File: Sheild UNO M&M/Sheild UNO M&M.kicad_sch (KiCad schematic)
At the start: 20 parts, among them J1 Power, J2 Analog, J3 Digital/PWM, J4 Digital/PWM, J5 Conn_01x02, J6 Conn_01x02, U1 HC05, U2 MCP41050, U4 LTC1050

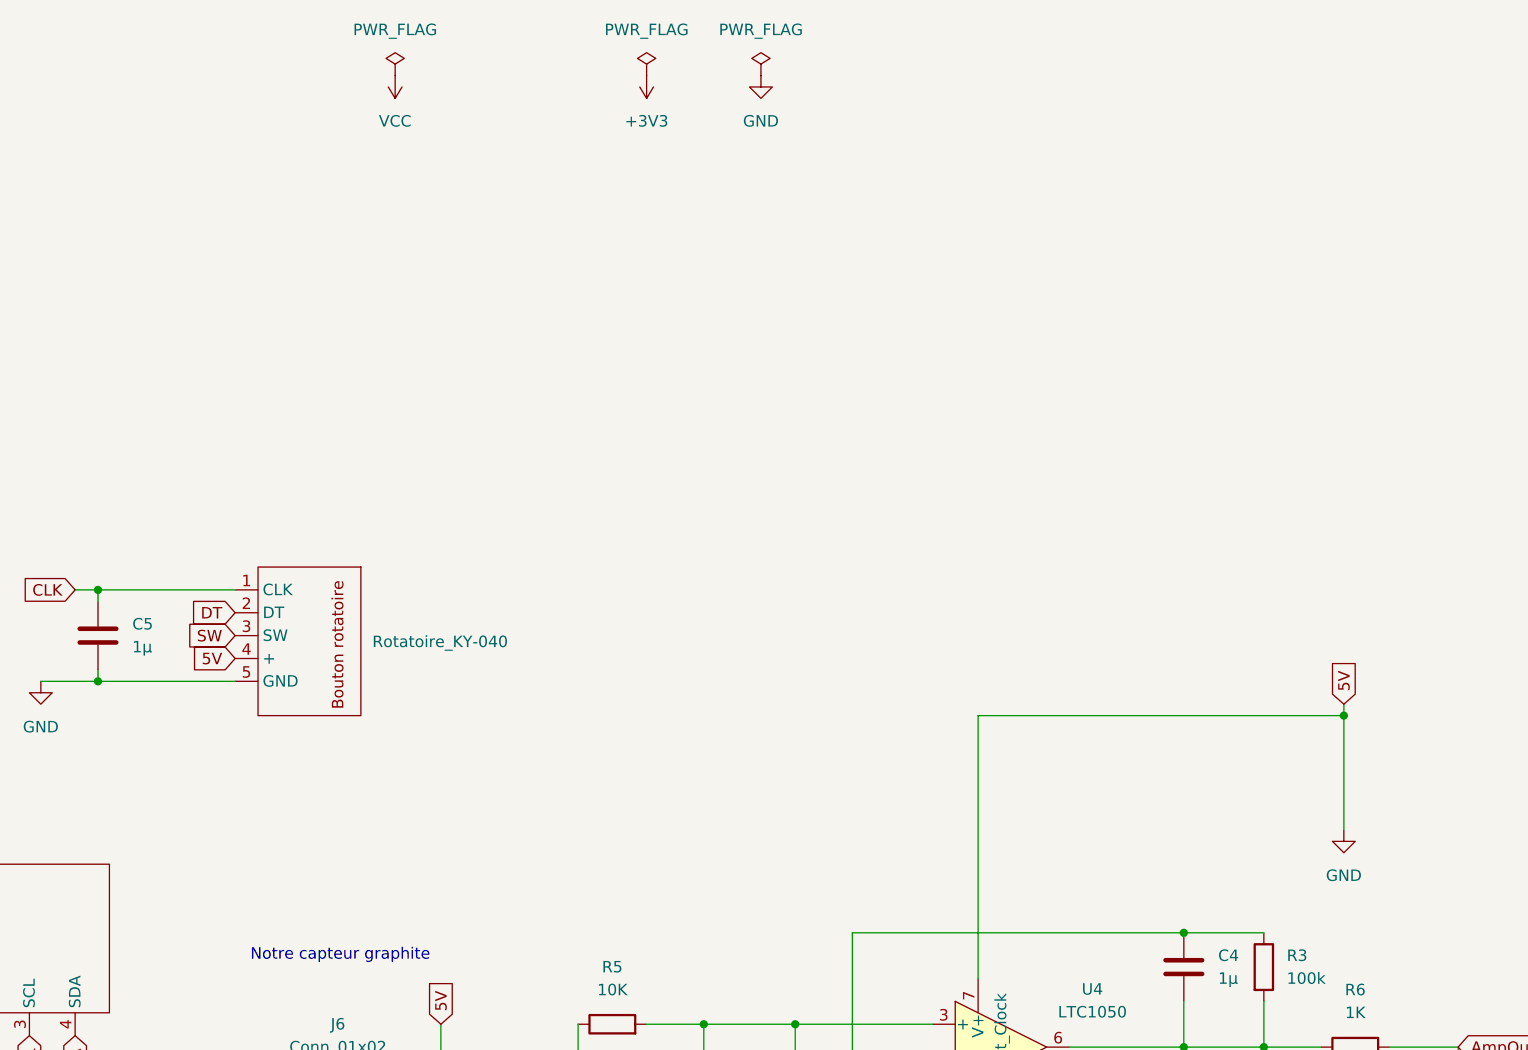
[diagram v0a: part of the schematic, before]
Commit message: Correction de l'erreur du GND connecté au 5V, continuer le routage
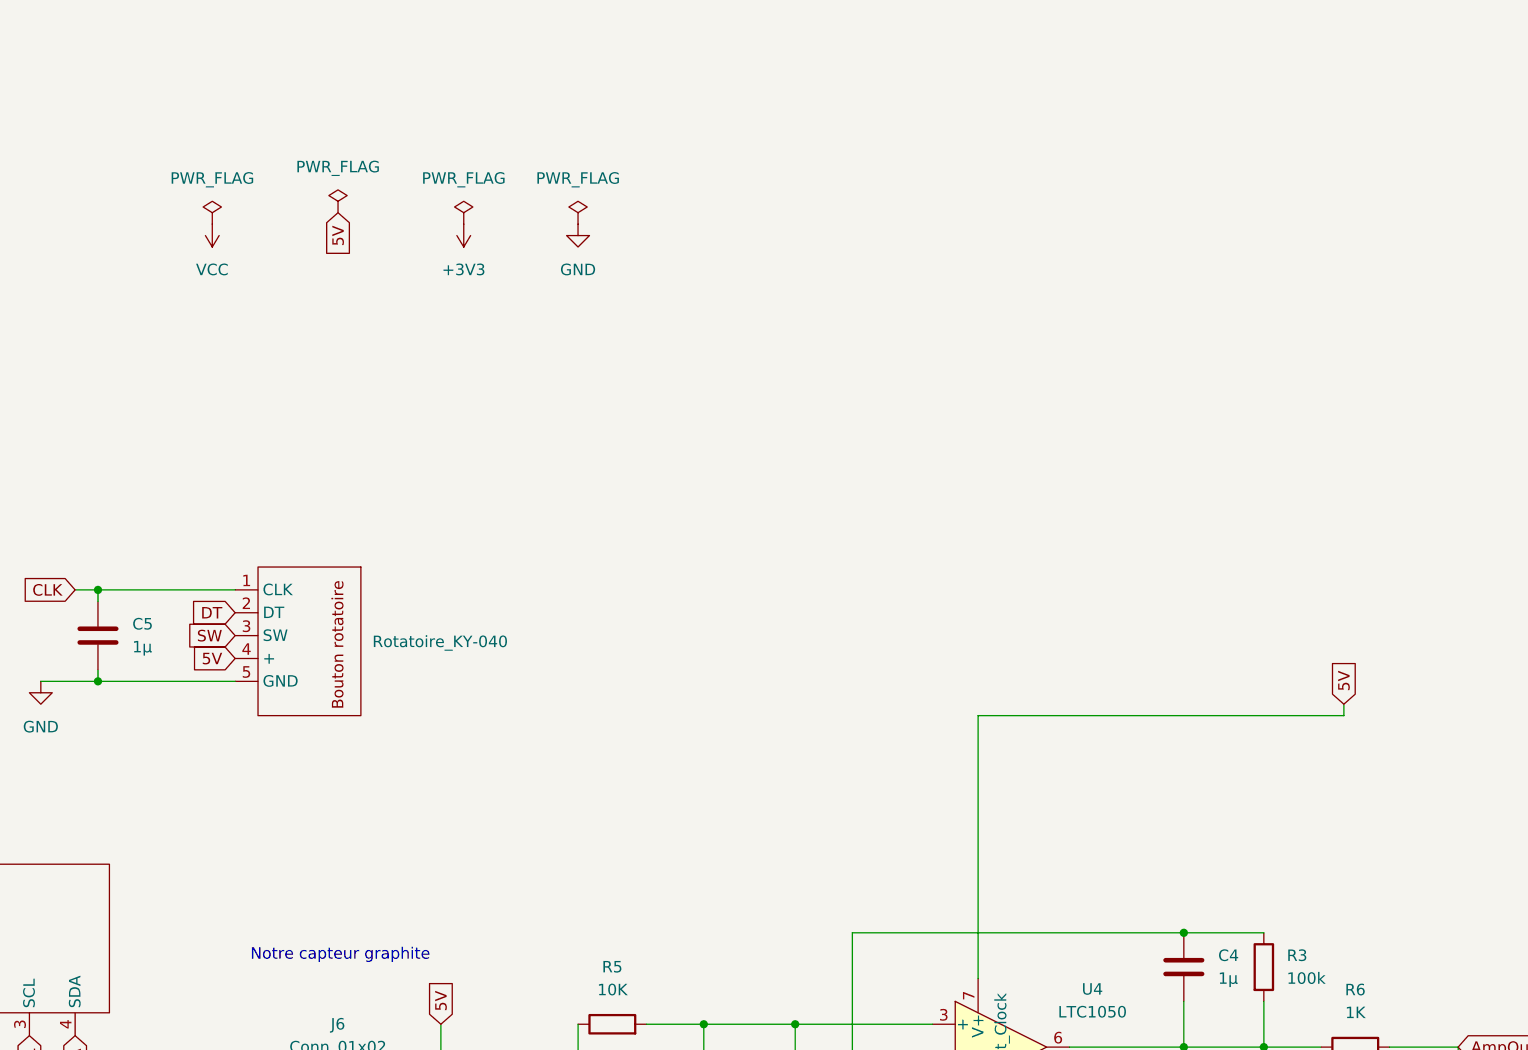
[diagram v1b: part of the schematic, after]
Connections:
- net GND: no longer 1.4 (+), DS1.2 (VCC), J1.5 (Pin_5), J5.2 (Pin_2), J6.2 (Pin_2), U1.2 (VCC), U2.8 (VDD), U4.7 (V+)
- new net 5V: 1.4 (+), DS1.2 (VCC), J1.5 (Pin_5), J5.2 (Pin_2), J6.2 (Pin_2), U1.2 (VCC), U2.8 (VDD), U4.7 (V+)
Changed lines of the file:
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@@
 	)
 	(junction
-		(at 255.27 93.98)
-		(diameter 0)
-		(color 0 0 0 0)
-	)
-	(junction
 		(at 200.66 133.35)
 		(diameter 0)
@@
 	(wire
 		(pts
-			(xy 255.27 93.98) (xy 255.27 106.68)
-		)
-		(stroke
-			(width 0)
-			(type default)
-		)
-	)
-	(wire
-		(pts
 			(xy 154.94 142.24) (xy 154.94 137.16)
 		)
@@
 	(global_label "5V"
 		(shape input)
+		(at 143.51 38.1 270)
+		(fields_autoplaced yes)
+		(effects
+			(font
+				(size 1.27 1.27)
+			)
+			(justify right)
+		)
+		(property "Intersheetrefs" "${INTERSHEET_REFS}"
+			(at 143.51 43.4784 90)
+			(effects
+				(font
+					(size 1.27 1.27)
+				)
+				(justify right)
+				(hide yes)
+			)
+		)
+	)
+	(global_label "5V"
+		(shape input)
 		(at 44.45 130.81 270)
 		(fields_autoplaced yes)
@@
 		(lib_name "GND_3")
 		(lib_id "power:GND")
-		(at 190.5 22.86 0)
+		(at 170.18 39.37 0)
 		(unit 1)
 		(exclude_from_sim no)
@@
 		(fields_autoplaced yes)
 		(property "Reference" "#PWR0113"
-			(at 190.5 29.21 0)
+			(at 170.18 45.72 0)
 			(effects
 				(font
@@
 		)
 		(property "Value" "GND"
-			(at 190.5 27.94 0)
+			(at 170.18 44.45 0)
 			(effects
 				(font
@@
 		)
 		(property "Footprint" ""
-			(at 190.5 22.86 0)
+			(at 170.18 39.37 0)
 			(effects
 				(font
@@
 		)
 		(property "Datasheet" ""
-			(at 190.5 22.86 0)
+			(at 170.18 39.37 0)
 			(effects
 				(font
@@
 		)
 		(property "Description" "Power symbol creates a global label with name \"GND\" , ground"
-			(at 190.5 22.86 0)
+			(at 170.18 39.37 0)
 			(effects
 				(font
@@
 		(lib_name "VCC_1")
 		(lib_id "power:VCC")
-		(at 149.86 22.86 180)
+		(at 129.54 39.37 180)
 		(unit 1)
 		(exclude_from_sim no)
@@
 		(fields_autoplaced yes)
 		(property "Reference" "#PWR0111"
-			(at 149.86 19.05 0)
+			(at 129.54 35.56 0)
 			(effects
 				(font
@@
 		)
 		(property "Value" "VCC"
-			(at 149.86 27.94 0)
+			(at 129.54 44.45 0)
 			(effects
 				(font
@@
 		)
 		(property "Footprint" ""
-			(at 149.86 22.86 0)
+			(at 129.54 39.37 0)
 			(effects
 				(font
@@
 		)
 		(property "Datasheet" ""
-			(at 149.86 22.86 0)
+			(at 129.54 39.37 0)
 			(effects
 				(font
@@
 		)
 		(property "Description" "Power symbol creates a global label with name \"VCC\""
-			(at 149.86 22.86 0)
+			(at 129.54 39.37 0)
 			(effects
 				(font
@@
 	(symbol
 		(lib_id "power:PWR_FLAG")
-		(at 177.8 22.86 0)
+		(at 157.48 39.37 0)
 		(unit 1)
 		(exclude_from_sim no)
@@
 		(fields_autoplaced yes)
 		(property "Reference" "#FLG0104"
-			(at 177.8 20.955 0)
+			(at 157.48 37.465 0)
 			(effects
 				(font
@@
 		)
 		(property "Value" "PWR_FLAG"
-			(at 177.8 17.78 0)
+			(at 157.48 34.29 0)
 			(effects
 				(font
@@
 		)
 		(property "Footprint" ""
-			(at 177.8 22.86 0)
+			(at 157.48 39.37 0)
 			(effects
 				(font
@@
 		)
 		(property "Datasheet" "~"
-			(at 177.8 22.86 0)
+			(at 157.48 39.37 0)
 			(effects
 				(font
@@
 		)
 		(property "Description" "Special symbol for telling ERC where power comes from"
-			(at 177.8 22.86 0)
+			(at 157.48 39.37 0)
 			(effects
 				(font
@@
 	)
 	(symbol
+		(lib_id "power:PWR_FLAG")
+		(at 143.51 38.1 0)
+		(unit 1)
+		(exclude_from_sim no)
+		(in_bom yes)
+		(on_board yes)
+		(dnp no)
+		(fields_autoplaced yes)
+		(property "Reference" "#FLG0105"
+			(at 143.51 36.195 0)
+			(effects
+				(font
+					(size 1.27 1.27)
+				)
+				(hide yes)
+			)
+		)
+		(property "Value" "PWR_FLAG"
+			(at 143.51 33.02 0)
+			(effects
+				(font
+					(size 1.27 1.27)
+				)
+			)
+		)
+		(property "Footprint" ""
+			(at 143.51 38.1 0)
+			(effects
+				(font
+					(size 1.27 1.27)
+				)
+				(hide yes)
+			)
+		)
+		(property "Datasheet" "~"
+			(at 143.51 38.1 0)
+			(effects
+				(font
+					(size 1.27 1.27)
+				)
+				(hide yes)
+			)
+		)
+		(property "Description" "Special symbol for telling ERC where power comes from"
+			(at 143.51 38.1 0)
+			(effects
+				(font
+					(size 1.27 1.27)
+				)
+				(hide yes)
+			)
+		)
+		(pin "1"
+		)
+		(instances
+			(project "Sheild UNO M&M"
+				(path "/e63e39d7-6ac0-4ffd-8aa3-1841a4541b55"
+					(reference "#FLG0105")
+					(unit 1)
+				)
+			)
+		)
+	)
+	(symbol
 		(lib_id "Device:R")
 		(at 173.99 128.27 90)
@@
 	(symbol
 		(lib_id "power:PWR_FLAG")
-		(at 149.86 22.86 0)
+		(at 129.54 39.37 0)
 		(unit 1)
 		(exclude_from_sim no)
@@
 		(fields_autoplaced yes)
 		(property "Reference" "#FLG0103"
-			(at 149.86 20.955 0)
+			(at 129.54 37.465 0)
 			(effects
 				(font
@@
 		)
 		(property "Value" "PWR_FLAG"
-			(at 149.86 17.78 0)
+			(at 129.54 34.29 0)
 			(effects
 				(font
@@
 		)
 		(property "Footprint" ""
-			(at 149.86 22.86 0)
+			(at 129.54 39.37 0)
 			(effects
 				(font
@@
 		)
 		(property "Datasheet" "~"
-			(at 149.86 22.86 0)
+			(at 129.54 39.37 0)
 			(effects
 				(font
@@
 		)
 		(property "Description" "Special symbol for telling ERC where power comes from"
-			(at 149.86 22.86 0)
+			(at 129.54 39.37 0)
 			(effects
 				(font
@@
 	)
 	(symbol
-		(lib_name "GND_1")
-		(lib_id "power:GND")
-		(at 255.27 106.68 0)
-		(unit 1)
-		(exclude_from_sim no)
-		(in_bom yes)
-		(on_board yes)
-		(dnp no)
-		(fields_autoplaced yes)
-		(property "Reference" "#PWR0109"
-			(at 255.27 113.03 0)
-			(effects
-				(font
-					(size 1.27 1.27)
-				)
-				(hide yes)
-			)
-		)
-		(property "Value" "GND"
-			(at 255.27 111.76 0)
-			(effects
-				(font
-					(size 1.27 1.27)
-				)
-			)
-		)
-		(property "Footprint" ""
-			(at 255.27 106.68 0)
-			(effects
-				(font
-					(size 1.27 1.27)
-				)
-				(hide yes)
-			)
-		)
-		(property "Datasheet" ""
-			(at 255.27 106.68 0)
-			(effects
-				(font
-					(size 1.27 1.27)
-				)
-				(hide yes)
-			)
-		)
-		(property "Description" "Power symbol creates a global label with name \"GND\" , ground"
-			(at 255.27 106.68 0)
-			(effects
-				(font
-					(size 1.27 1.27)
-				)
-				(hide yes)
-			)
-		)
-		(pin "1"
-		)
-		(instances
-			(project "Sheild UNO M&M"
-				(path "/e63e39d7-6ac0-4ffd-8aa3-1841a4541b55"
-					(reference "#PWR0109")
-					(unit 1)
-				)
-			)
-		)
-	)
-	(symbol
 		(lib_name "+3V3_1")
 		(lib_id "power:+3V3")
-		(at 177.8 22.86 180)
+		(at 157.48 39.37 180)
 		(unit 1)
 		(exclude_from_sim no)
@@
 		(fields_autoplaced yes)
 		(property "Reference" "#PWR0112"
-			(at 177.8 19.05 0)
+			(at 157.48 35.56 0)
 			(effects
 				(font
@@
 		)
 		(property "Value" "+3V3"
-			(at 177.8 27.94 0)
+			(at 157.48 44.45 0)
 			(effects
 				(font
@@
 		)
 		(property "Footprint" ""
-			(at 177.8 22.86 0)
+			(at 157.48 39.37 0)
 			(effects
 				(font
@@
 		)
 		(property "Datasheet" ""
-			(at 177.8 22.86 0)
+			(at 157.48 39.37 0)
 			(effects
 				(font
@@
 		)
 		(property "Description" "Power symbol creates a global label with name \"+3V3\""
-			(at 177.8 22.86 0)
+			(at 157.48 39.37 0)
 			(effects
 				(font
@@
 	(symbol
 		(lib_id "power:PWR_FLAG")
-		(at 190.5 22.86 0)
+		(at 170.18 39.37 0)
 		(unit 1)
 		(exclude_from_sim no)
@@
 		(fields_autoplaced yes)
 		(property "Reference" "#FLG0102"
-			(at 190.5 20.955 0)
+			(at 170.18 37.465 0)
 			(effects
 				(font
@@
 		)
 		(property "Value" "PWR_FLAG"
-			(at 190.5 17.78 0)
+			(at 170.18 34.29 0)
 			(effects
 				(font
@@
 		)
 		(property "Footprint" ""
-			(at 190.5 22.86 0)
+			(at 170.18 39.37 0)
 			(effects
 				(font
@@
 		)
 		(property "Datasheet" "~"
-			(at 190.5 22.86 0)
+			(at 170.18 39.37 0)
 			(effects
 				(font
@@
 		)
 		(property "Description" "Special symbol for telling ERC where power comes from"
-			(at 190.5 22.86 0)
+			(at 170.18 39.37 0)
 			(effects
 				(font

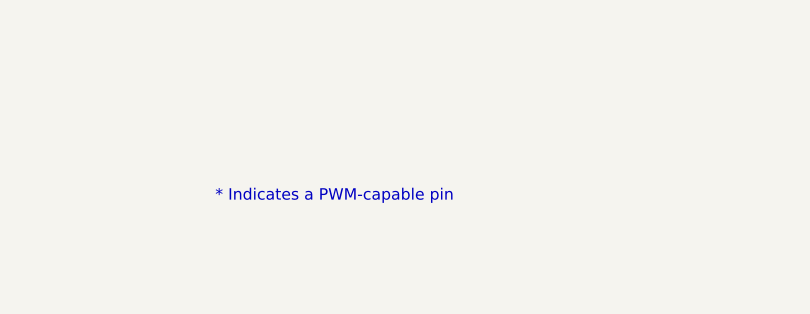
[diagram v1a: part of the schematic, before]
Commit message: Rajout de nos noms sur le shield
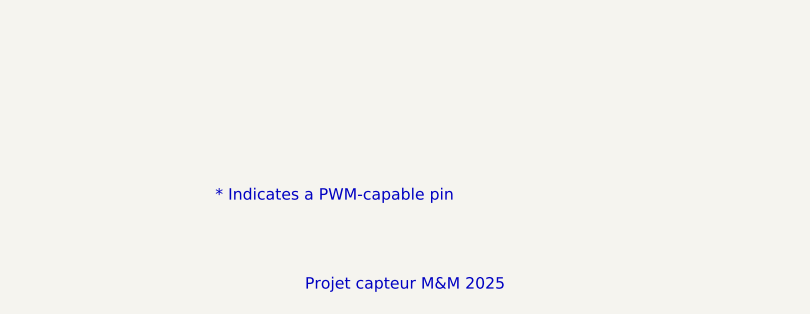
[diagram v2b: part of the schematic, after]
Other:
- note added: "Projet capteur M&M 2025"
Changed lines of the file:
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@@
+		)
+	)
+	(text "Projet capteur M&M 2025"
+		(exclude_from_sim no)
+		(at 198.882 189.484 0)
+		(effects
+			(font
+				(size 1.27 1.27)
+			)
 		)
 	)

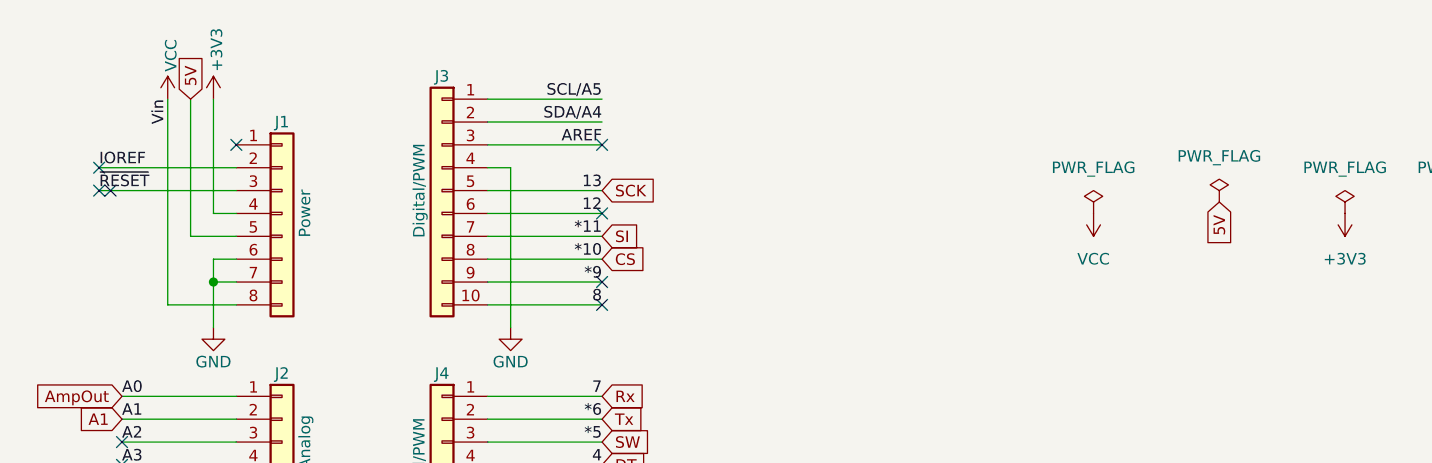
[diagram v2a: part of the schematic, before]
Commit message: Corrections PCB sur les empreintes des connecteurs et amélioration des via
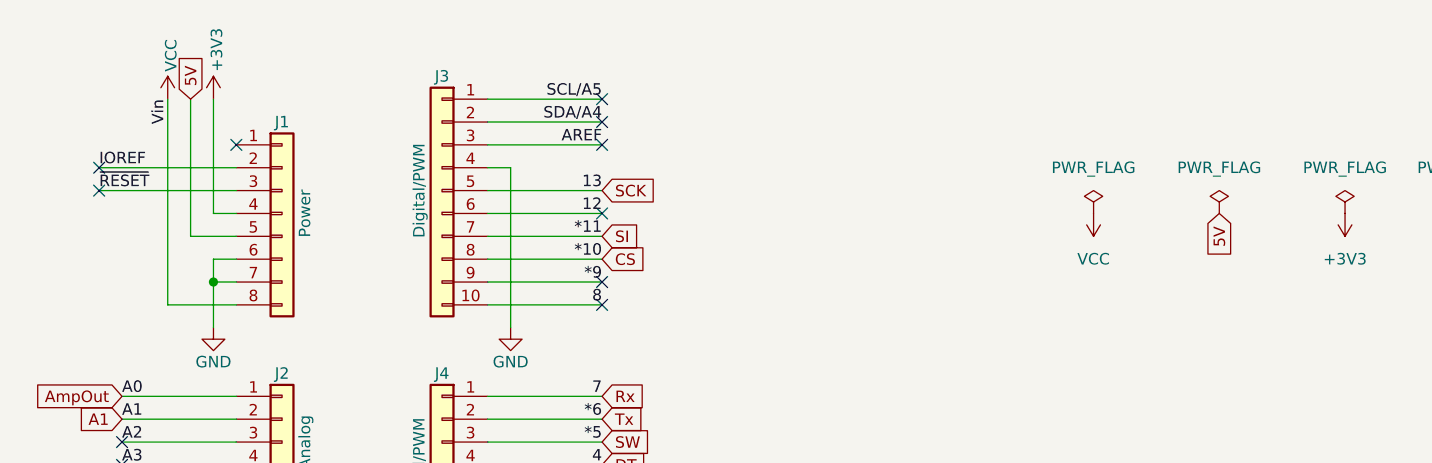
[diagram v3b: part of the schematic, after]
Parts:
- J5, J6: footprint Une_Librairie_d_empreinte:PinSocket_1x02_P2.54mm_Vertical_Header_Empreinte -> Une_Librairie_d_empreinte:PinSocket_1x02_P2.54mm_Vertical_Modifié
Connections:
- no-connect marks 16 -> 17
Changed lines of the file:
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@@
 	)
 	(no_connect
-		(at 20.32 36.83)
+		(at 74.93 26.67)
 	)
 	(no_connect
@@
 	)
 	(no_connect
+		(at 74.93 29.21)
+	)
+	(no_connect
 		(at 21.59 64.77)
 	)
@@
 	(global_label "5V"
 		(shape input)
-		(at 143.51 38.1 270)
+		(at 143.51 39.37 270)
 		(fields_autoplaced yes)
 		(effects
@@
 		)
 		(property "Intersheetrefs" "${INTERSHEET_REFS}"
-			(at 143.51 43.4784 90)
+			(at 143.51 44.7484 90)
 			(effects
 				(font
@@
 			)
 		)
-		(property "Footprint" "Une_Librairie_d_empreinte:PinSocket_1x02_P2.54mm_Vertical_Header_Empreinte"
+		(property "Footprint" "Une_Librairie_d_empreinte:PinSocket_1x02_P2.54mm_Vertical_Modifié"
 			(at 143.51 137.16 0)
 			(effects
@@
 	(symbol
 		(lib_id "power:PWR_FLAG")
-		(at 143.51 38.1 0)
+		(at 143.51 39.37 0)
 		(unit 1)
 		(exclude_from_sim no)
@@
 		(fields_autoplaced yes)
 		(property "Reference" "#FLG0105"
-			(at 143.51 36.195 0)
+			(at 143.51 37.465 0)
 			(effects
 				(font
@@
 		)
 		(property "Value" "PWR_FLAG"
-			(at 143.51 33.02 0)
+			(at 143.51 34.29 0)
 			(effects
 				(font
@@
 		)
 		(property "Footprint" ""
-			(at 143.51 38.1 0)
+			(at 143.51 39.37 0)
 			(effects
 				(font
@@
 		)
 		(property "Datasheet" "~"
-			(at 143.51 38.1 0)
+			(at 143.51 39.37 0)
 			(effects
 				(font
@@
 		)
 		(property "Description" "Special symbol for telling ERC where power comes from"
-			(at 143.51 38.1 0)
+			(at 143.51 39.37 0)
 			(effects
 				(font
@@
 			)
 		)
-		(property "Footprint" "Une_Librairie_d_empreinte:PinSocket_1x02_P2.54mm_Vertical_Header_Empreinte"
+		(property "Footprint" "Une_Librairie_d_empreinte:PinSocket_1x02_P2.54mm_Vertical_Modifié"
 			(at 106.68 170.18 0)
 			(effects

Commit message: Correction PCB et ajout des modèles 3D
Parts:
- U4: footprint Package_DIP:DIP-8_W7.62mm -> Une_Librairie_d_empreinte:Potentiometre MCP41050
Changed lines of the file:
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@@
 			)
 		)
-		(property "Footprint" "Package_DIP:DIP-8_W7.62mm"
+		(property "Footprint" "Une_Librairie_d_empreinte:Potentiometre MCP41050"
 			(at 218.948 113.284 0)
 			(effects
